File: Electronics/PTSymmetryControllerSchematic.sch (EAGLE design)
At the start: 28 parts, among them IC1 MIC2954, IC2 PIC16F18323, T1 2N3055, T2 2N3055

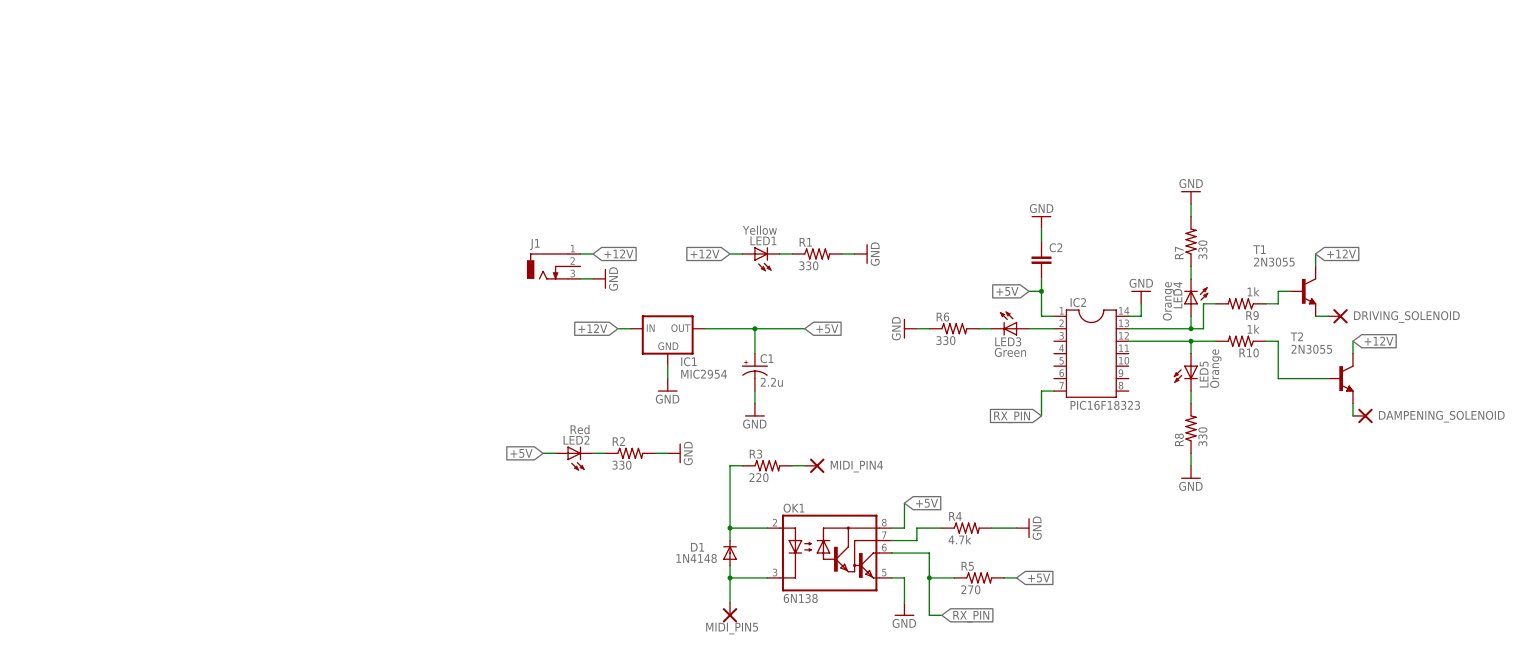
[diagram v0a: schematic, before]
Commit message: Removed unneeded library file and updated schematic to include better LED indicators, ICSP, and more stable circuiry
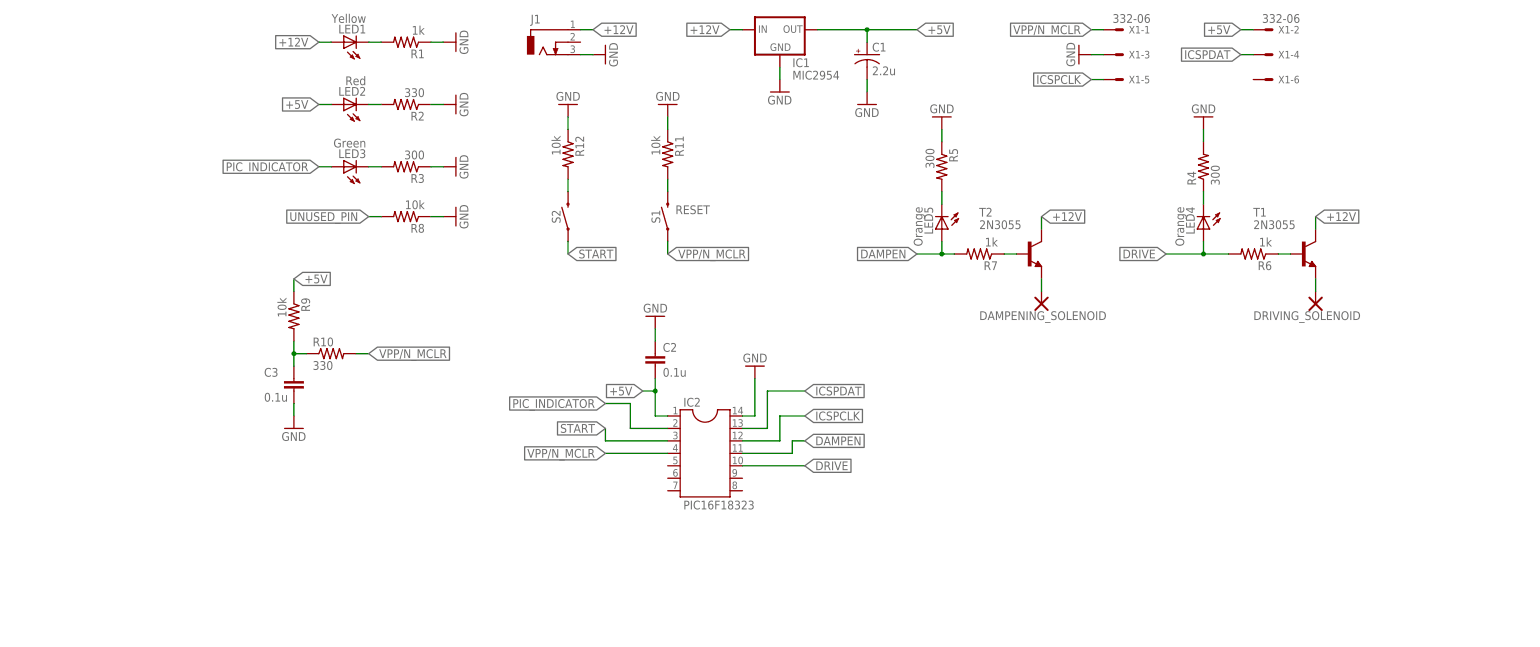
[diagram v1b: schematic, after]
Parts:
- removed D1: 1N4148, diode:1N4148DO35-10
- removed MIDI_PIN4, MIDI_PIN5: DOUBLE_THROUGH_HOLE_PAD, DOUBLE_THROUGH_HOLE_PAD:DOUBLE_THROUGH_HOLE_PAD
- removed OK1: 6N138, optocoupler:6N138
- added C3: 0.1u, capacitor-wima:C5/2.5
- added R11, R12: 10k, rcl:R-US_0207/10
- added S1: RESET, SparkFun-Switches:MOMENTARY-SWITCH-SPST-PTH-6.0MM
- added S2: START, SparkFun-Switches:MOMENTARY-SWITCH-SPST-PTH-6.0MM
- added X1: 332-06, con-garry:332-06
- C2: value (none) -> 0.1u
- R1, R6, R7: value 330 -> 1k
- R10: value 1k -> 330
- R3: value 220 -> 300
- R4: value 4.7k -> 300
- R5: value 270 -> 300
- R8: value 330 -> 10k
- R9: value 1k -> 10k
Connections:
- net N$5 renamed PIC_INDICATOR
- removed net N$10: IC2.12, LED5.A, R10.2
- removed net N$4: D1.A, MIDI_PIN5.P$1, OK1.C
- removed net N$7: OK1.VB, R4.1
- removed net N$9: IC2.13, LED4.A, R9.2
- removed net RX_PIN: IC2.7, OK1.VO, R5.1
- new net DAMPEN: IC2.11, LED5.A, R7.2
- new net DRIVE: IC2.10, LED4.A, R6.2
- new net ICSPCLK: IC2.12, X1-5.S
- new net ICSPDAT: IC2.13, X1-4.S
- new net N$5: R11.2, S1.2
- new net START: IC2.3, S2.1
- new net UNUSED_PIN: R8.2
- new net VPP/N_MCLR: IC2.4, R10.2, S1.1, X1-1.S
- net +5V: now also R9.1, X1-2.S; no longer OK1.VCC, R5.2
- net GND: now also C3.2, R1.1, R11.1, R12.1, R2.1, R3.1, R5.1, X1-3.S; no longer OK1.GND, R1.2, R2.2, R6.1, R7.2
- net N$1: now also LED1.C, R1.2; no longer LED2.C, R2.1
- net N$11: now also R4.1; no longer R7.1
- net N$12: now also R5.2; no longer R8.2
- net N$15: now also R6.1; no longer R9.1
- net N$16: now also R7.1; no longer R10.1
- net N$2: now also LED2.C, R2.2; no longer LED1.C, R1.1
- net N$3: now also C3.1, R10.1, R9.2; no longer D1.C, OK1.A, R3.1
- net N$6: now also R12.2, S2.2; no longer MIDI_PIN4.P$1, R3.2
- net N$8: now also R3.2; no longer R6.2
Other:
- moved on the sheet: C1, C2, DAMPENING_SOLENOID, DRIVING_SOLENOID, IC1, IC2, J1, LED1, LED2, LED3, LED4, LED5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

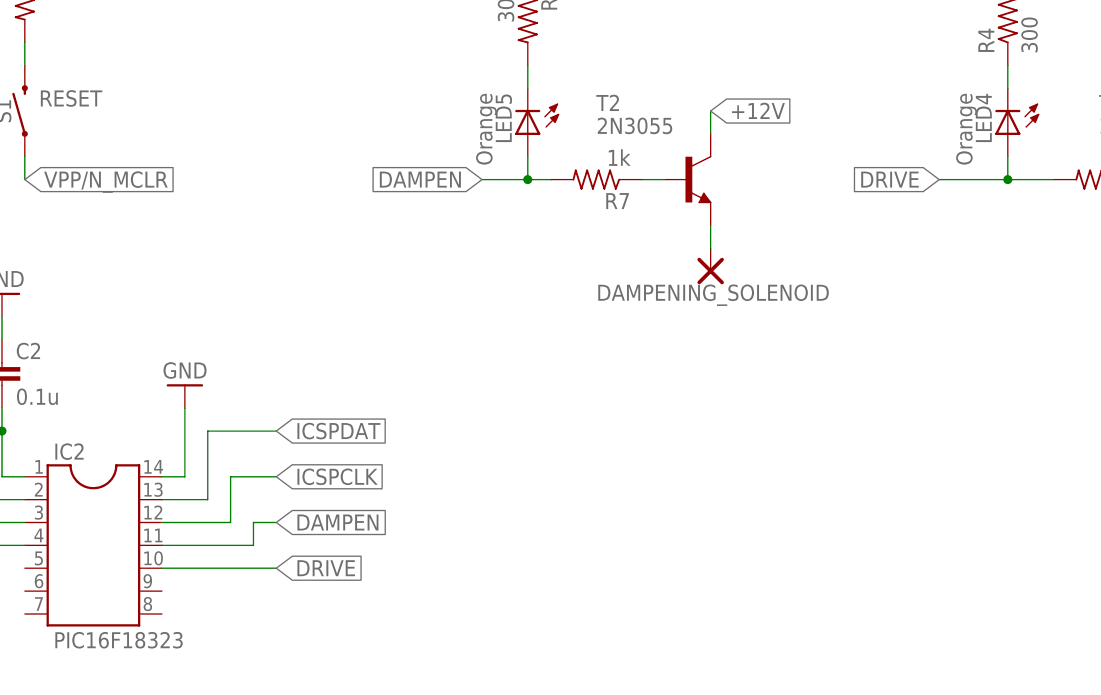
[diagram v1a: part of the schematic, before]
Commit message: Made MPLAB project for firmware and updated photogate inputs in schematic
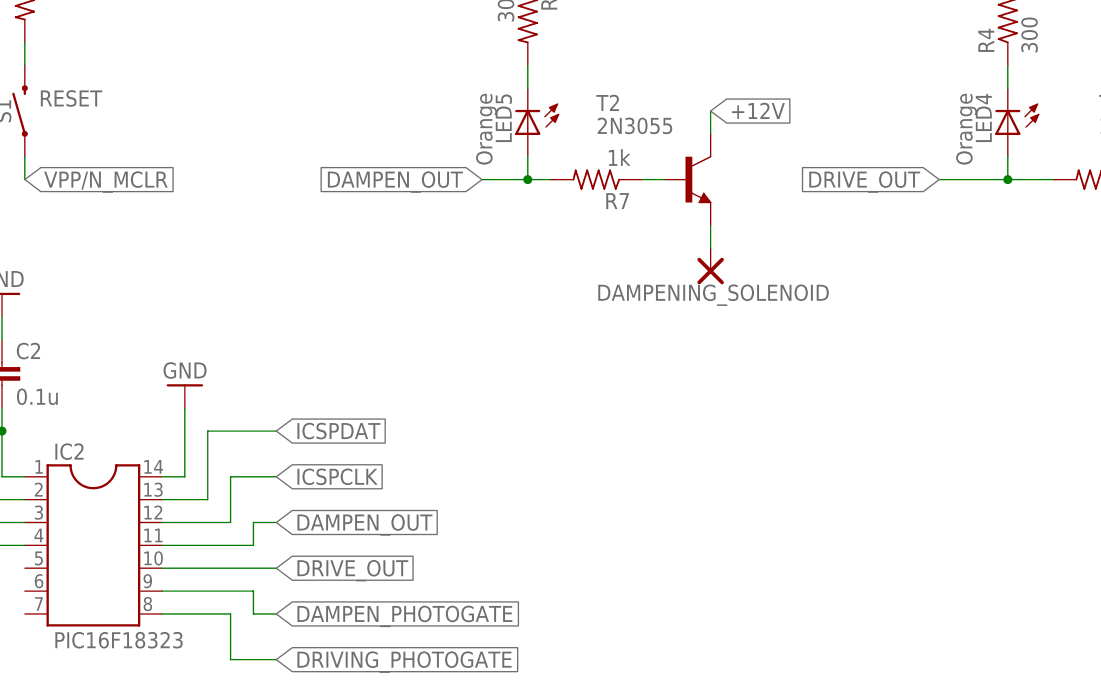
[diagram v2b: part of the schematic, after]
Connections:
- net DAMPEN renamed DAMPEN_OUT
- net DRIVE renamed DRIVE_OUT
- new net DAMPEN_PHOTOGATE: IC2.9
- new net DRIVING_PHOTOGATE: IC2.8

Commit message: Correctly named photogate tag
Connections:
- net DAMPEN_PHOTOGATE renamed DAMPENING_PHOTOGATE
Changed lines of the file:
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@@
 </segment>
 </net>
-<net name="DAMPEN_PHOTOGATE" class="0">
+<net name="DAMPENING_PHOTOGATE" class="0">
 <segment>
 <pinref part="IC2" gate="G$1" pin="9"/>

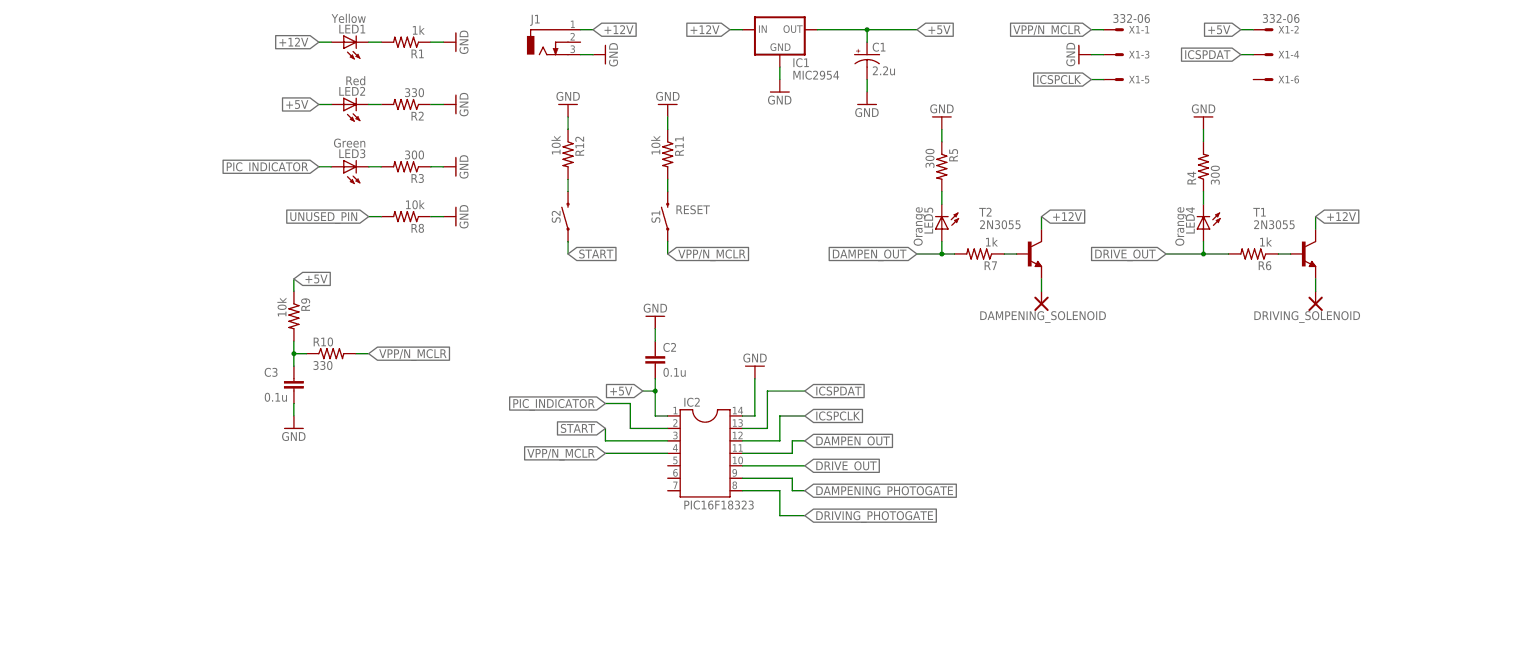
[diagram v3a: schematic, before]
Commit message: Added "photogates" to circuit
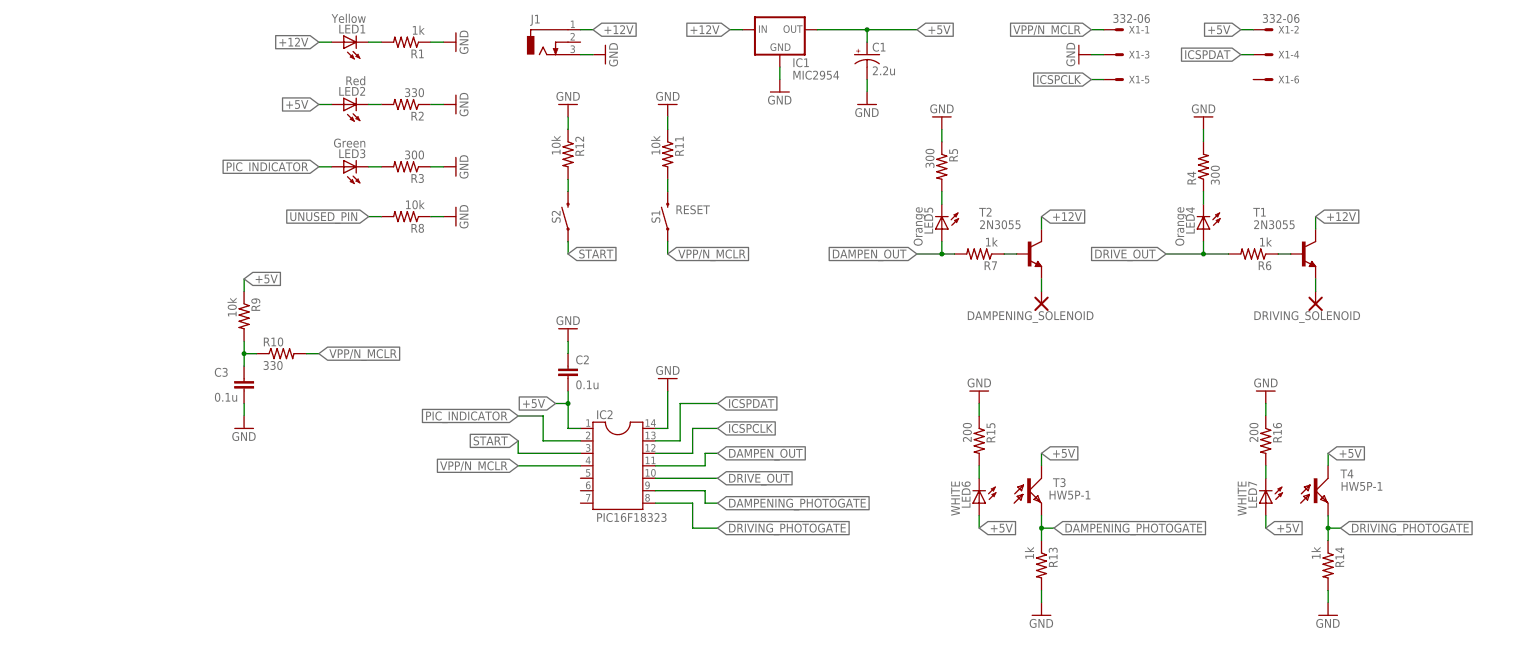
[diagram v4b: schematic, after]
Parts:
- added LED6, LED7: WHITE, led:LED3MM
- added R13, R14: 1k, rcl:R-US_0207/10
- added R15, R16: 200, rcl:R-US_0207/10
- added T3, T4: HW5P-1, opto-trans-siemens:BPX81
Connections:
- new net N$4: LED6.C, R15.2
- new net N$9: LED7.C, R16.2
- net +5V: now also LED6.A, LED7.A, T3.C, T4.C
- net DAMPENING_PHOTOGATE: now also R13.1, T3.E
- net DRIVING_PHOTOGATE: now also R14.1, T4.E
- net GND: now also R13.2, R14.2, R15.1, R16.1
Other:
- moved on the sheet: C2, C3, IC2, R10, R9

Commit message: Started cleaning up schematic and grouping subcircuits.
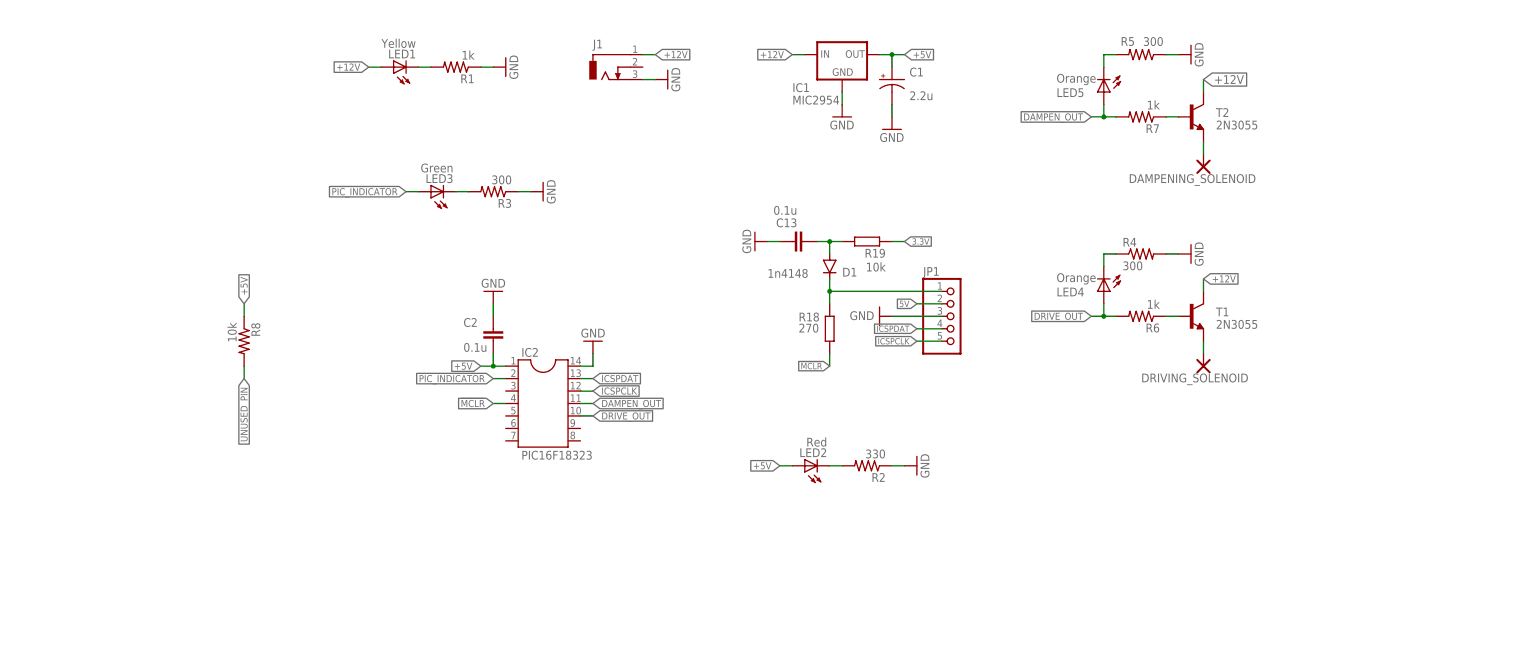
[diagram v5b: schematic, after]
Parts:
- removed C3: 0.1u, capacitor-wima:C5/2.5
- removed LED6, LED7: WHITE, led:LED3MM
- removed R10: 330, rcl:R-US_0207/10
- removed R11, R12, R9: 10k, rcl:R-US_0207/10
- removed R13, R14: 1k, rcl:R-US_0207/10
- removed R15, R16: 200, rcl:R-US_0207/10
- removed S1: RESET, SparkFun-Switches:MOMENTARY-SWITCH-SPST-PTH-6.0MM
- removed S2: START, SparkFun-Switches:MOMENTARY-SWITCH-SPST-PTH-6.0MM
- removed T3, T4: HW5P-1, opto-trans-siemens:BPX81
- removed X1: 332-06, con-garry:332-06
- added C13: 0.1u, resistor:C-EUC0603
- added D1: 1n4148, diode:DIODE-SOD123
- added JP1: 1x5x2mm-pinheader, pinhead:PINHD-1X55X2MM
- added R18: 270, resistor:R-EU_R0603
- added R19: 10k, resistor:R-EU_R0603
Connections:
- removed net DAMPENING_PHOTOGATE: IC2.9, R13.1, T3.E
- removed net DRIVING_PHOTOGATE: IC2.8, R14.1, T4.E
- removed net N$3: C3.1, R10.1, R9.2
- removed net N$4 (its old number): LED6.C, R15.2
- removed net N$5 (its old number): R11.2, S1.2
- removed net N$9: LED7.C, R16.2
- removed net START: IC2.3, S2.1
- removed net VPP/N_MCLR: IC2.4, R10.2, S1.1, X1-1.S
- new net !MCLR: IC2.4, R18.2
- new net 3.3V: R19.1
- new net 5V: JP1.2
- new net N$7: D1.C, JP1.1, R18.1
- net +5V: now also R8.1; no longer LED6.A, LED7.A, R9.1, T3.C, T4.C, X1-2.S
- net GND: now also C13.1, JP1.3; no longer C3.2, R11.1, R12.1, R13.2, R14.2, R15.1, R16.1, R8.1, X1-3.S
- net ICSPCLK: now also JP1.5; no longer X1-5.S
- net ICSPDAT: now also JP1.4; no longer X1-4.S
- net N$6: now also C13.2, D1.A, R19.2; no longer R12.2, S2.2
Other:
- moved on the sheet: C1, C2, DAMPENING_SOLENOID, DRIVING_SOLENOID, IC1, IC2, J1, LED1, LED2, LED3, LED4, LED5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

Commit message: Finished schematic. Passed ERC.
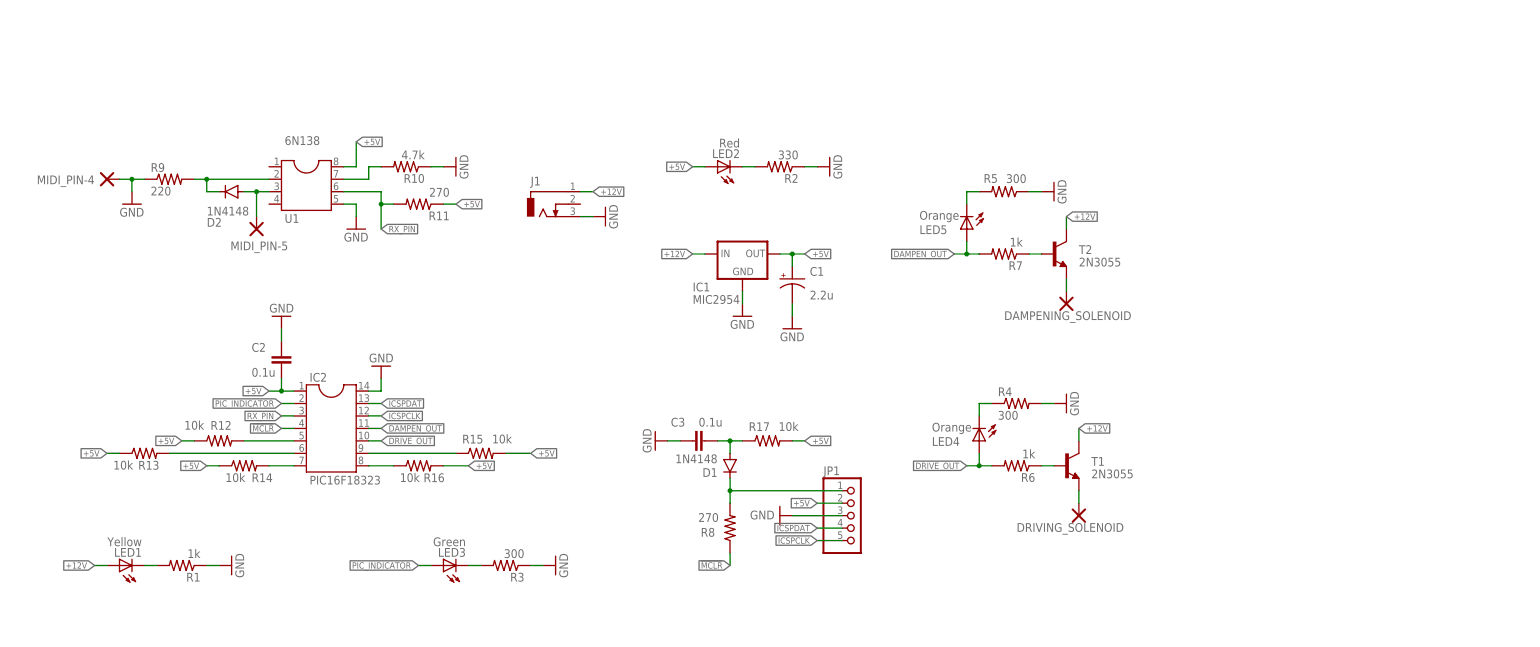
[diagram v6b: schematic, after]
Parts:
- removed C13: 0.1u, resistor:C-EUC0603
- removed R18: 270, resistor:R-EU_R0603
- removed R19: 10k, resistor:R-EU_R0603
- added 6N138: U1, ic-package:DIL8S
- added C3: 0.1u, capacitor-wima:C5/2.5
- added D2: 1N4148, diode:1N4148DO35-10
- added MIDI_PIN-4, MIDI_PIN-5: DOUBLE_THROUGH_HOLE_PAD, Double-Through-Hole-Pad:DOUBLE_THROUGH_HOLE_PAD
- added R10: 4.7k, resistor:R-US_0207/12
- added R11: 270, resistor:R-US_0207/12
- added R12, R13, R14, R15, R16, R17: 10k, rcl:R-US_0207/10
- added R9: 220, resistor:R-US_0207/12
- D1: value 1n4148 -> 1N4148; device diode:DIODE-SOD123 -> diode:1N4148DO35-10
- DAMPENING_SOLENOID, DRIVING_SOLENOID: device DOUBLE_THROUGH_HOLE_PAD:DOUBLE_THROUGH_HOLE_PAD -> Double-Through-Hole-Pad:DOUBLE_THROUGH_HOLE_PAD
- JP1: device pinhead:PINHD-1X55X2MM -> pinhead:PINHD-1X5
- R8: value 10k -> 270
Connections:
- removed net 3.3V: R19.1
- removed net 5V: JP1.2
- removed net UNUSED_PIN: R8.2
- new net MIDI_PIN-5: 6N138.3, D2.A, MIDI_PIN-5.P$1
- new net N$10: IC2.5, R12.2
- new net N$11: IC2.6, R13.2
- new net N$12: IC2.7, R14.2
- new net N$14: IC2.9, R15.1
- new net N$17: IC2.8, R16.1
- new net N$3: 6N138.7, R10.2
- new net N$9: 6N138.2, D2.C, R9.2
- new net RX_PIN: 6N138.6, IC2.3, R11.2
- net !MCLR: now also R8.1; no longer R18.2
- net +5V: now also 6N138.8, JP1.2, R11.1, R12.1, R13.1, R14.1, R15.2, R16.2, R17.2; no longer R8.1
- net GND: now also 6N138.5, C3.1, MIDI_PIN-4.P$1, R10.1, R9.1; no longer C13.1
- net N$6: now also C3.2, R17.1; no longer C13.2, R19.2
- net N$7: now also R8.2; no longer R18.1
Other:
- moved on the sheet: C1, C2, D1, DAMPENING_SOLENOID, DRIVING_SOLENOID, IC1, IC2, J1, JP1, LED1, LED2, LED3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
